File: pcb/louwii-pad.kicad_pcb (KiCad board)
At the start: 2 copper layers, 88 x 106 mm, 50 parts, among them J1 USB_B_Mini, J2 ICSP, J3 IIC, K1 KEYSW, K2 KEYSW, K3 KEYSW, K4 KEYSW, K5 KEYSW, K6 KEYSW, K7 KEYSW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

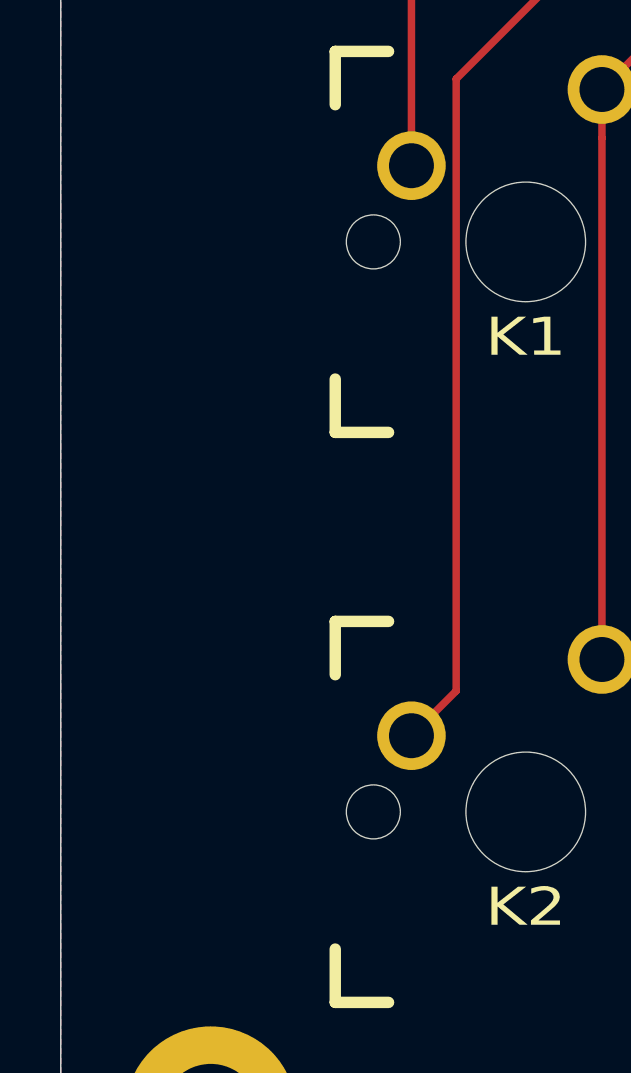
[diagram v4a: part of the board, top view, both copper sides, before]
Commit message: add logo and rev on PCB
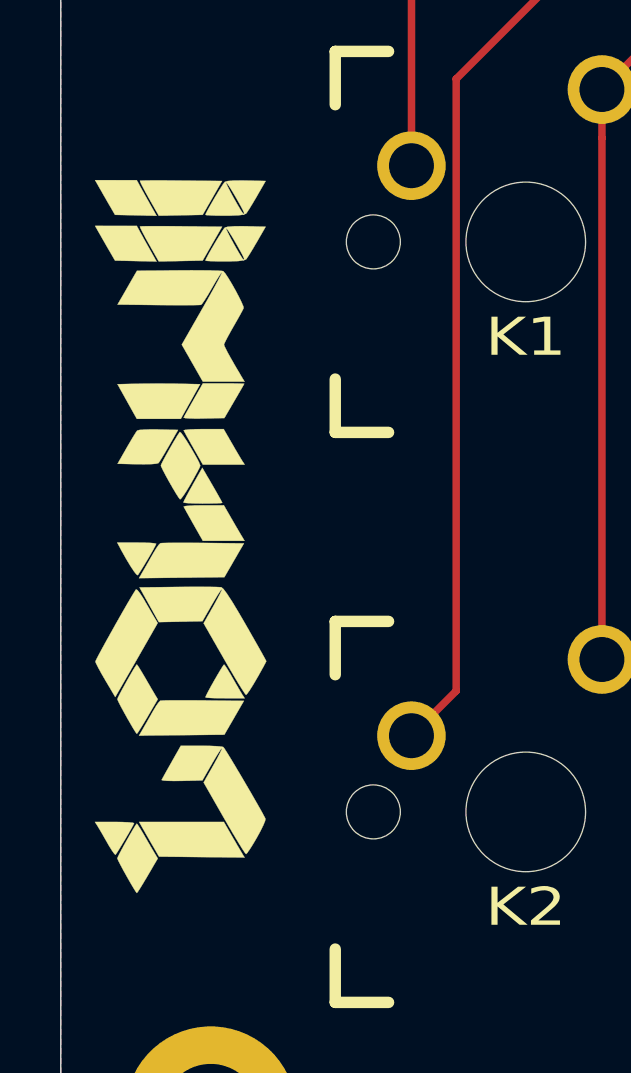
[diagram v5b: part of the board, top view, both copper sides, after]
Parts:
- added G***: LOGO, Louwii-pad:LouWii-logo, F.Cu at (114.2, 119.2)
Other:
- board text added: "Louwii pad - rev. 1"
